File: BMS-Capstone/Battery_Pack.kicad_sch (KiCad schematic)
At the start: 16 parts, among them J1 Conn_01x02_Socket, J2 Conn_01x02_Socket, J3 Conn_01x13_Socket, K1 J107F1CS203VDC.80

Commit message: Final touches
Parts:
- J3: footprint Connector_PinHeader_2.54mm:PinHeader_1x13_P2.54mm_Vertical -> Connector_JST:JST_XH_S13B-XH-A-1_1x13_P2.50mm_Horizontal
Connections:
- net GND renamed PACKGND
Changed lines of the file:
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@@
 			)
 		)
-		(property "Value" "GND"
+		(property "Value" "PACKGND"
 			(at 134.62 184.15 0)
 			(effects
@@
 			)
 		)
-		(property "Footprint" "Connector_PinHeader_2.54mm:PinHeader_1x13_P2.54mm_Vertical"
+		(property "Footprint" "Connector_JST:JST_XH_S13B-XH-A-1_1x13_P2.50mm_Horizontal"
 			(at 50.8 109.22 0)
 			(effects
@@
 			)
 		)
-		(property "Value" "GND"
+		(property "Value" "PACKGND"
 			(at 139.7 43.18 0)
 			(effects

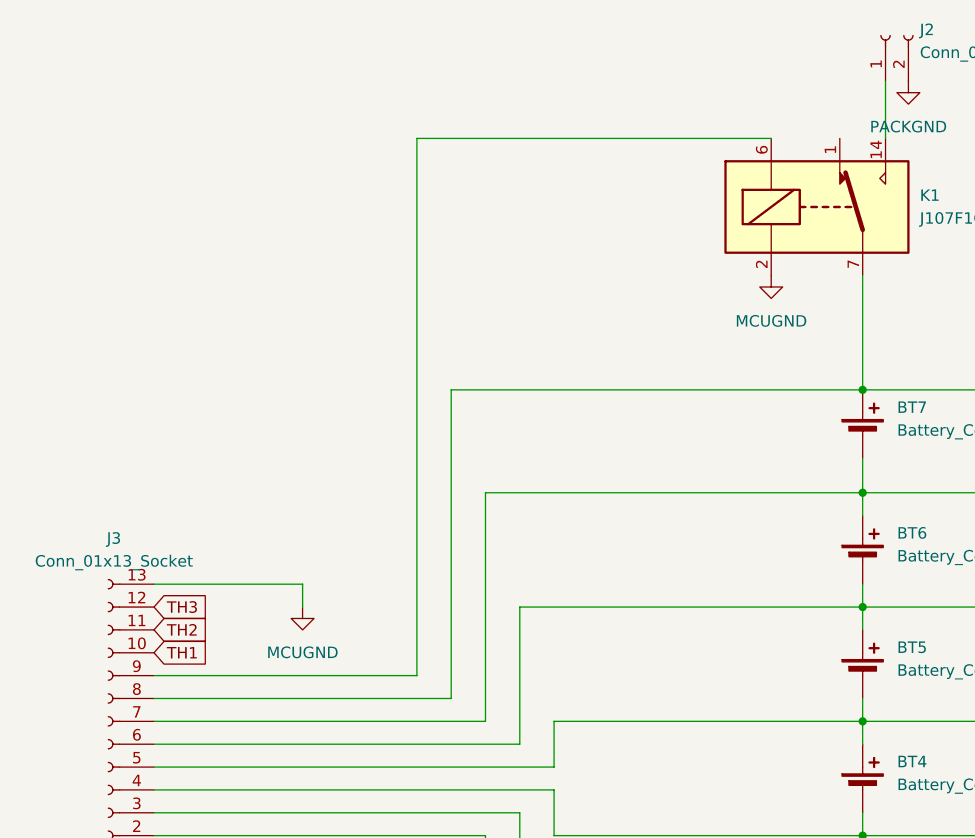
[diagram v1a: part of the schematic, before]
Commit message: Added Transistors for optocouple and relay drive
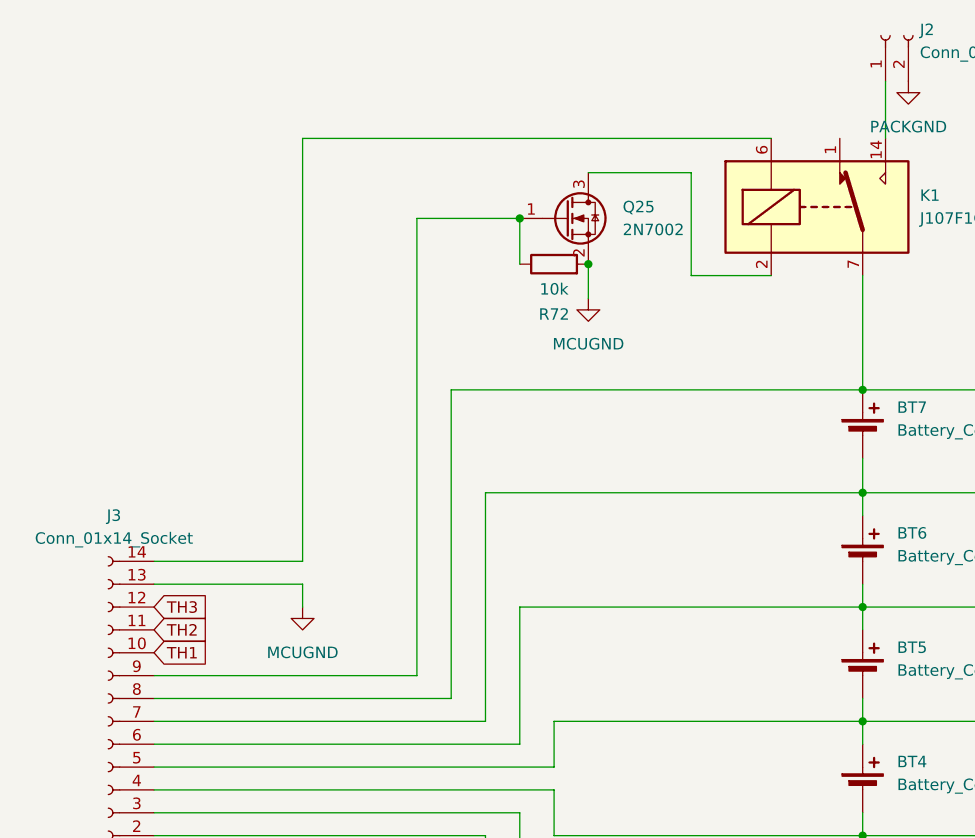
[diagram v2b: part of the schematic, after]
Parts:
- removed J3: Conn_01x13_Socket, Connector_JST:JST_XH_S13B-XH-A-1_1x13_P2.50mm_Horizontal, symbol Connector:Conn_01x13_Socket
- added J3: Conn_01x14_Socket, Connector_JST:JST_XH_S14B-XH-A-1_1x14_P2.50mm_Horizontal, symbol Connector:Conn_01x14_Socket
- added Q25: 2N7002, Package_TO_SOT_SMD:SOT-23, symbol Transistor_FET:2N7002
- added R72: 10k, Resistor_SMD:R_0805_2012Metric, symbol Device:R
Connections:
- net 1+: now also J3.2 (Pin_2)
- net 1-: now also J3.1 (Pin_1)
- net 2+: now also J3.3 (Pin_3)
- net 3+: now also J3.4 (Pin_4)
- net 4+: now also J3.5 (Pin_5)
- net 5+: now also J3.6 (Pin_6)
- net 6+: now also J3.7 (Pin_7)
- net 7+: now also J3.8 (Pin_8)
- net MCUGND: now also J3.13 (Pin_13), Q25.2 (S), R72.2; no longer K1.2
- net TH1: now also J3.10 (Pin_10)
- net TH2: now also J3.11 (Pin_11)
- net TH3: now also J3.12 (Pin_12)
- net at K1.6: now also J3.14 (Pin_14)
- new net: J3.9 (Pin_9), Q25.1 (G), R72.1
- new net: K1.2, Q25.3 (D)
